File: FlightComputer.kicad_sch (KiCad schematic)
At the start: 0 parts

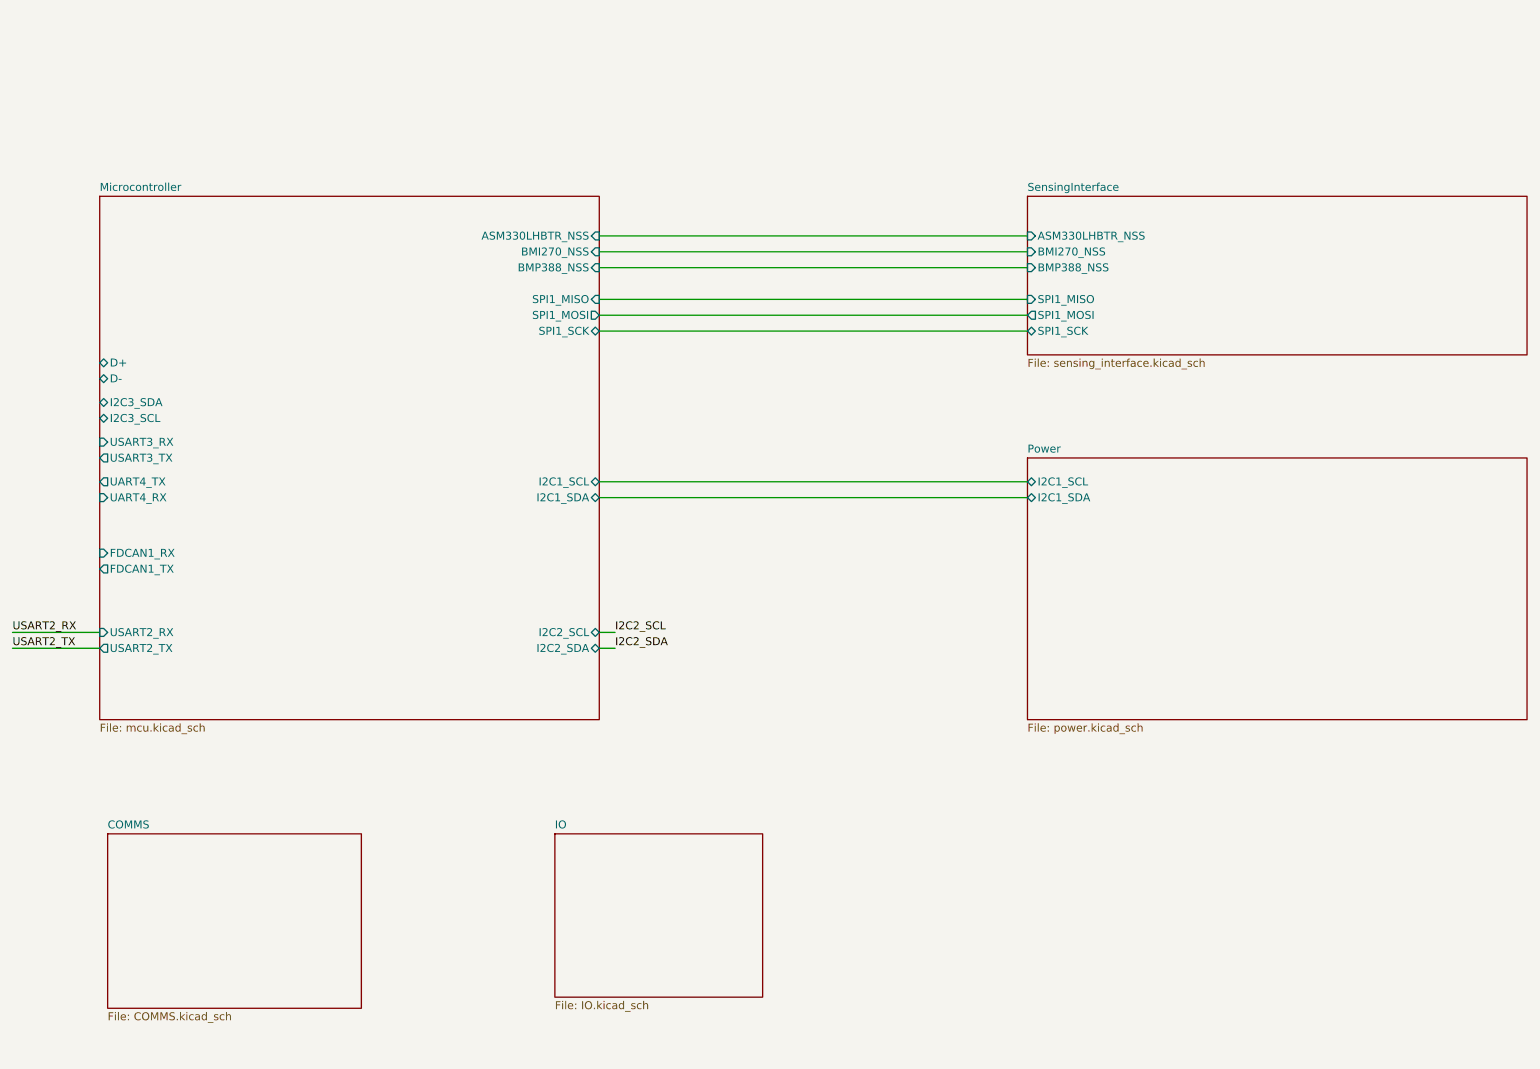
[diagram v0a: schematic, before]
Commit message: corrections and IO updated
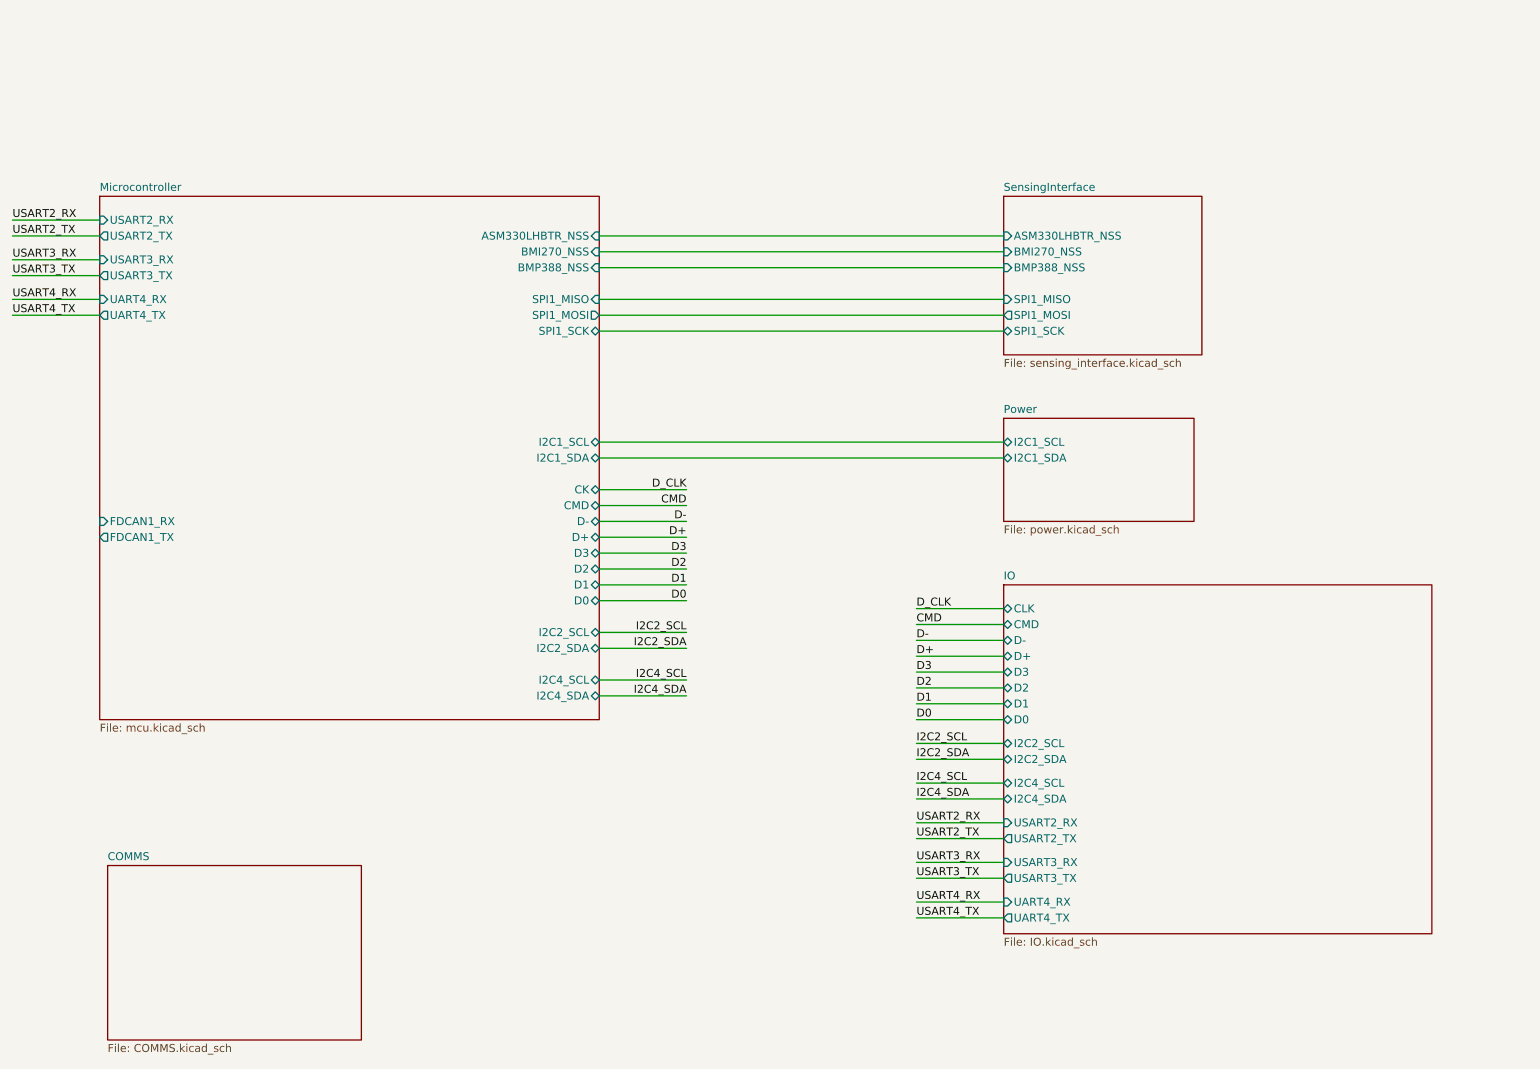
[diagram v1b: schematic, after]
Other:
- sheet IO ports: added CLK, CMD, D+, D-, D0, D1, D2, D3, I2C2_SCL, I2C2_SDA, I2C4_SCL, I2C4_SDA, UART4_RX, UART4_TX, USART2_RX, USART2_TX, USART3_RX, USART3_TX; removed none
- sheet Microcontroller ports: added CK, CMD, D0, D1, D2, D3, I2C4_SCL, I2C4_SDA; removed I2C3_SCL, I2C3_SDA

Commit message: mcu updates
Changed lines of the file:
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@@
 	)
 	(sheet
-		(at 34.29 151.638)
+		(at 33.274 148.59)
 		(size 40.64 27.94)
 		(exclude_from_sim no)
@@
 		)
 		(property "Sheetname" "COMMS"
-			(at 34.29 150.9264 0)
+			(at 33.274 147.8784 0)
 			(show_name no)
 			(do_not_autoplace no)
@@
 		)
 		(property "Sheetfile" "COMMS.kicad_sch"
-			(at 34.29 180.1626 0)
+			(at 33.274 177.1146 0)
 			(show_name no)
 			(do_not_autoplace no)

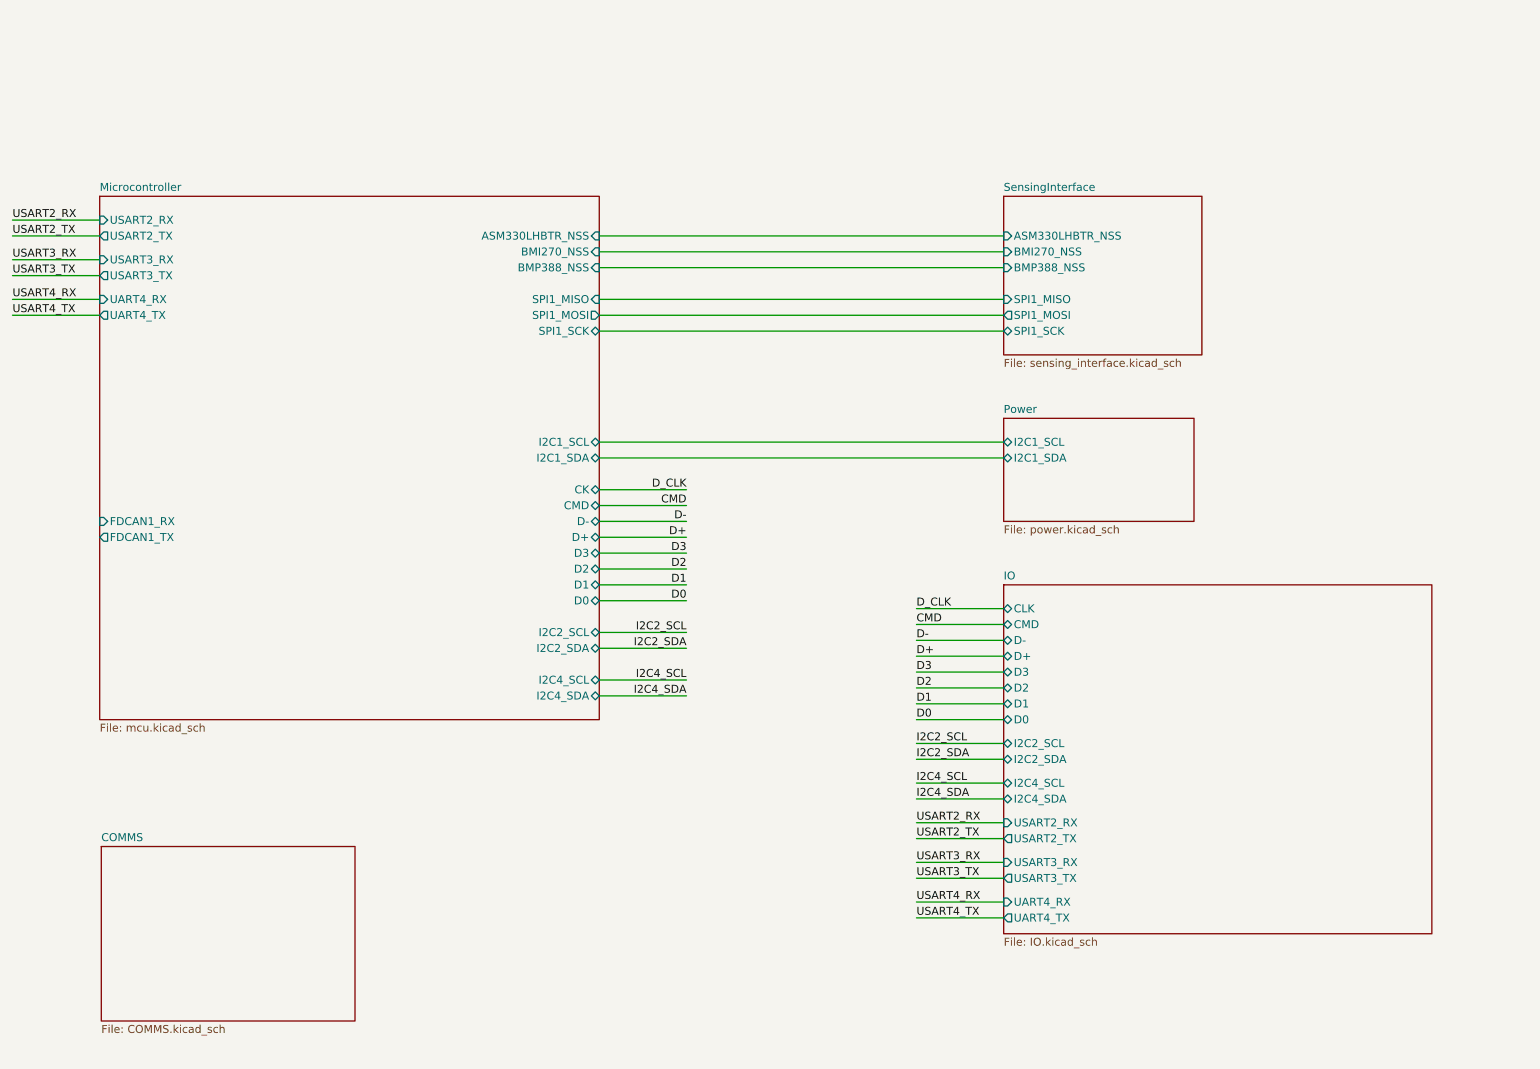
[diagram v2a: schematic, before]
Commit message: added in RF componentys and updated and reviewed STM connections
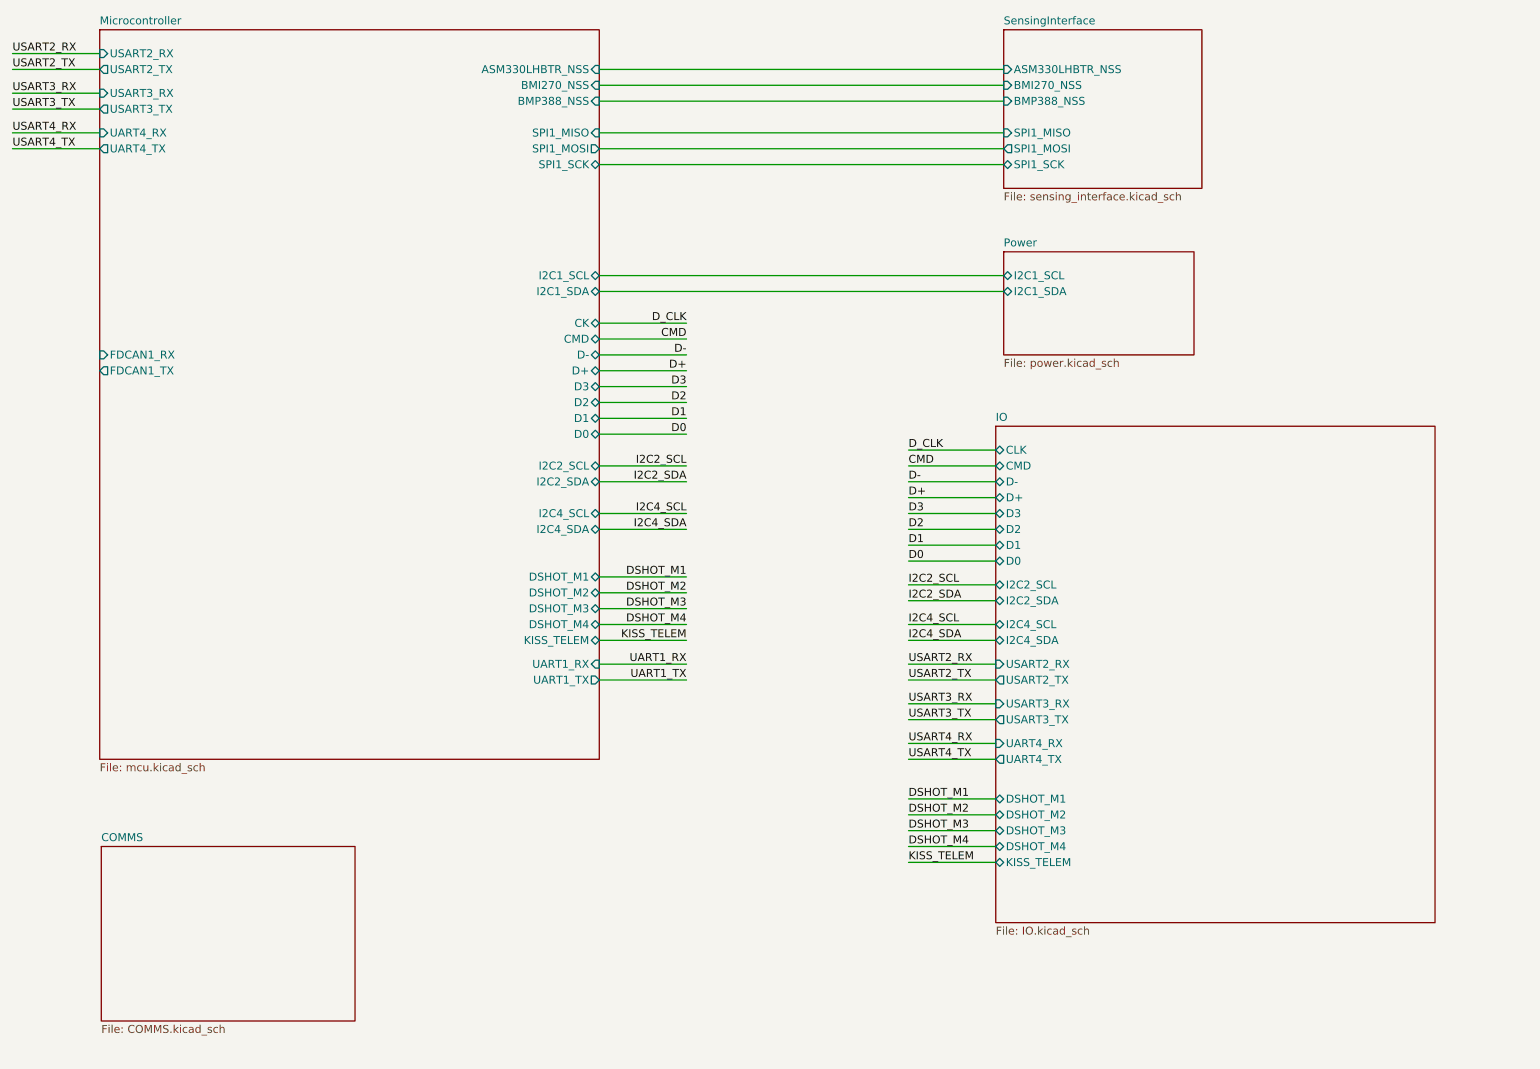
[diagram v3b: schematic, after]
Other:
- sheet IO ports: added DSHOT_M1, DSHOT_M2, DSHOT_M3, DSHOT_M4, KISS_TELEM; removed none
- sheet Microcontroller ports: added DSHOT_M1, DSHOT_M2, DSHOT_M3, DSHOT_M4, KISS_TELEM, UART1_RX, UART1_TX; removed none

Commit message: finalized RF
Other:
- sheet COMMS ports: added UART1_RX, UART1_TX; removed none
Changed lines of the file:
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@@
+	(wire
+		(pts
+			(xy 73.66 156.21) (xy 93.98 156.21)
+		)
+		(stroke
+			(width 0)
+			(type default)
+		)
+	)
 	(wire
 		(pts
@@
 		(pts
 			(xy 162.56 109.22) (xy 176.53 109.22)
+		)
+		(stroke
+			(width 0)
+			(type default)
+		)
+	)
+	(wire
+		(pts
+			(xy 73.66 153.67) (xy 93.98 153.67)
 		)
 		(stroke
@@
 		)
 	)
+	(label "UART1_RX"
+		(at 93.98 153.67 180)
+		(effects
+			(font
+				(size 1.27 1.27)
+			)
+			(justify right bottom)
+		)
+	)
 	(label "D2"
 		(at 127 77.47 180)
@@
 	(label "DSHOT_M4"
 		(at 127 113.03 180)
+		(effects
+			(font
+				(size 1.27 1.27)
+			)
+			(justify right bottom)
+		)
+	)
+	(label "UART1_TX"
+		(at 93.98 156.21 180)
 		(effects
 			(font
@@
 	)
 	(sheet
-		(at 33.274 148.59)
+		(at 33.02 148.59)
 		(size 40.64 27.94)
 		(exclude_from_sim no)
@@
 		)
 		(property "Sheetname" "COMMS"
-			(at 33.274 147.8784 0)
+			(at 33.02 147.8784 0)
 			(show_name no)
 			(do_not_autoplace no)
@@
 		)
 		(property "Sheetfile" "COMMS.kicad_sch"
-			(at 33.274 177.1146 0)
+			(at 33.02 177.1146 0)
 			(show_name no)
 			(do_not_autoplace no)
@@
 			)
 		)
+		(pin "UART1_RX" input
+			(at 73.66 153.67 0)
+			(effects
+				(font
+					(size 1.27 1.27)
+				)
+				(justify right)
+			)
+		)
+		(pin "UART1_TX" input
+			(at 73.66 156.21 0)
+			(effects
+				(font
+					(size 1.27 1.27)
+				)
+				(justify right)
+			)
+		)
